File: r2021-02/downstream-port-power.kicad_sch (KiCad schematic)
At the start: 31 parts, among them J10 USB_A_DUAL, J4 USB_A (female down), J6 USB_A_DUAL, J7 USB_A_DUAL, U10 NUP4202, U11 NUP4202, U13 NUP4202, U14 NUP4202, U15 NUP4202, U16 NUP4202, U17 NUP4202, U3 USB2517, U4 APL3511C, U5 APL3511C, U6 APL3511C, U7 APL3511C, U8 APL3511C, U9 APL3511C

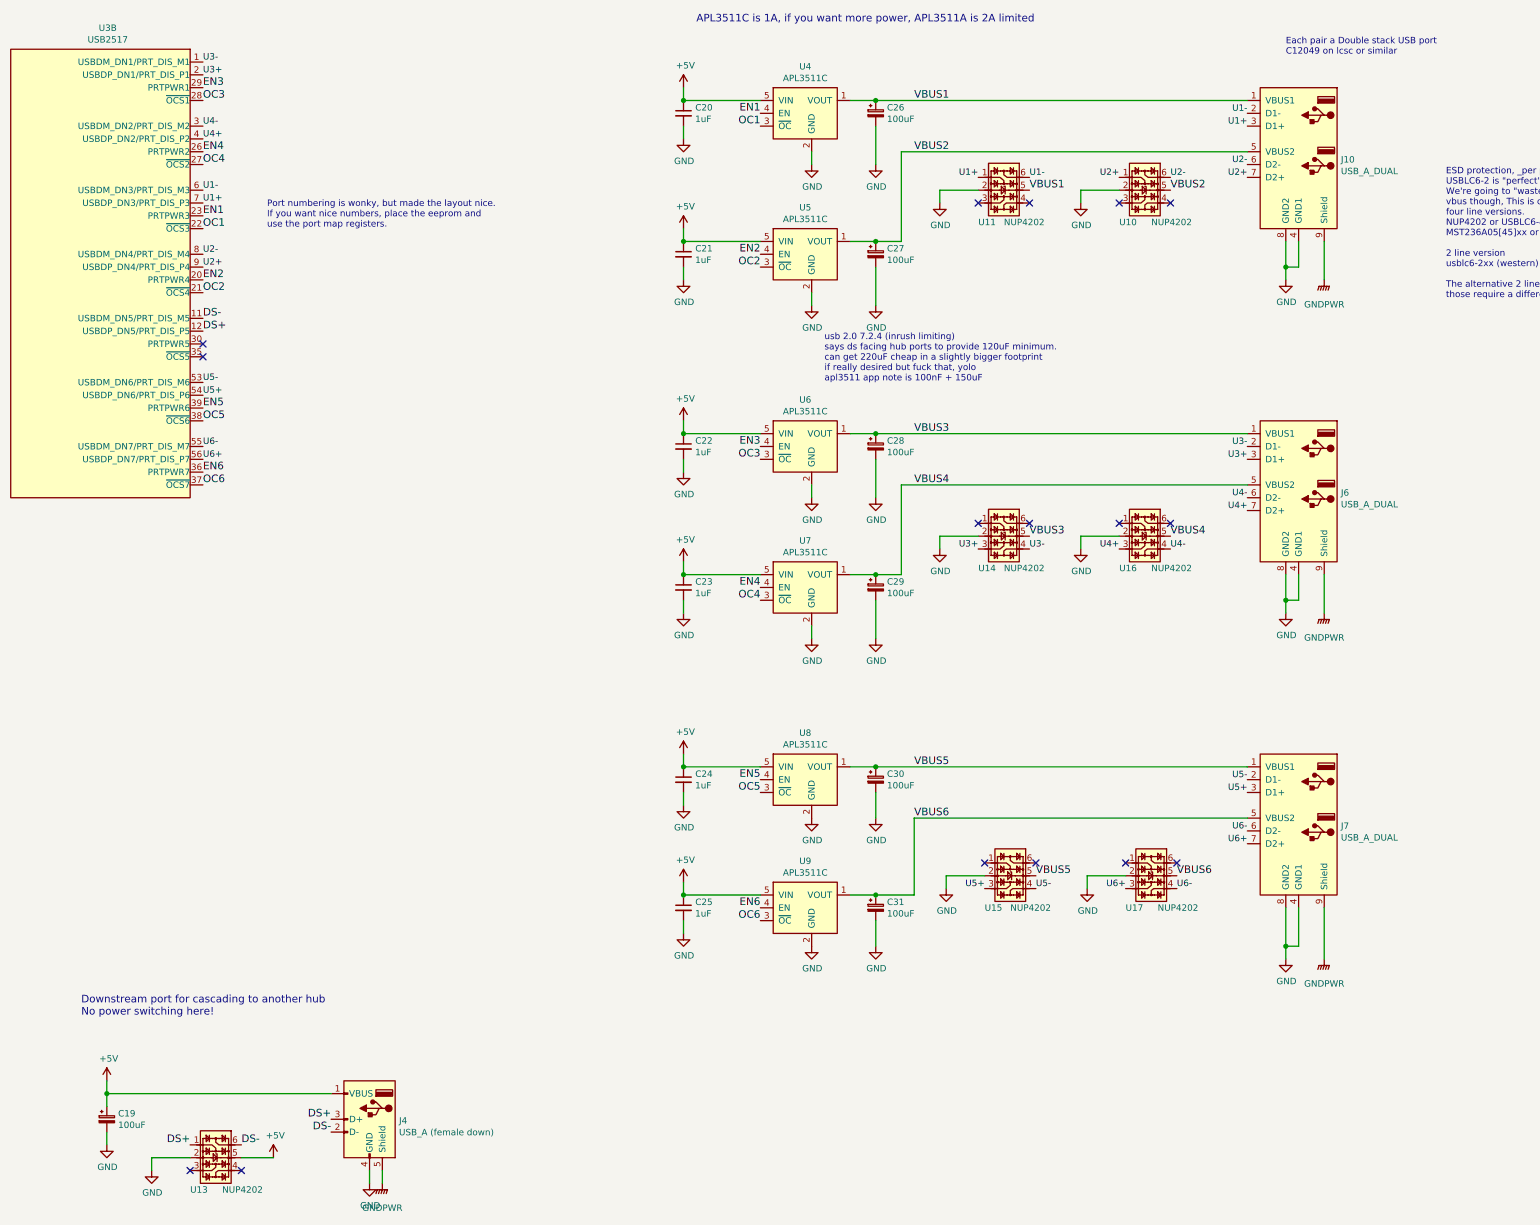
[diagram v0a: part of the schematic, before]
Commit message: switch to upstream dual usb symbol
less private local parts, more better.
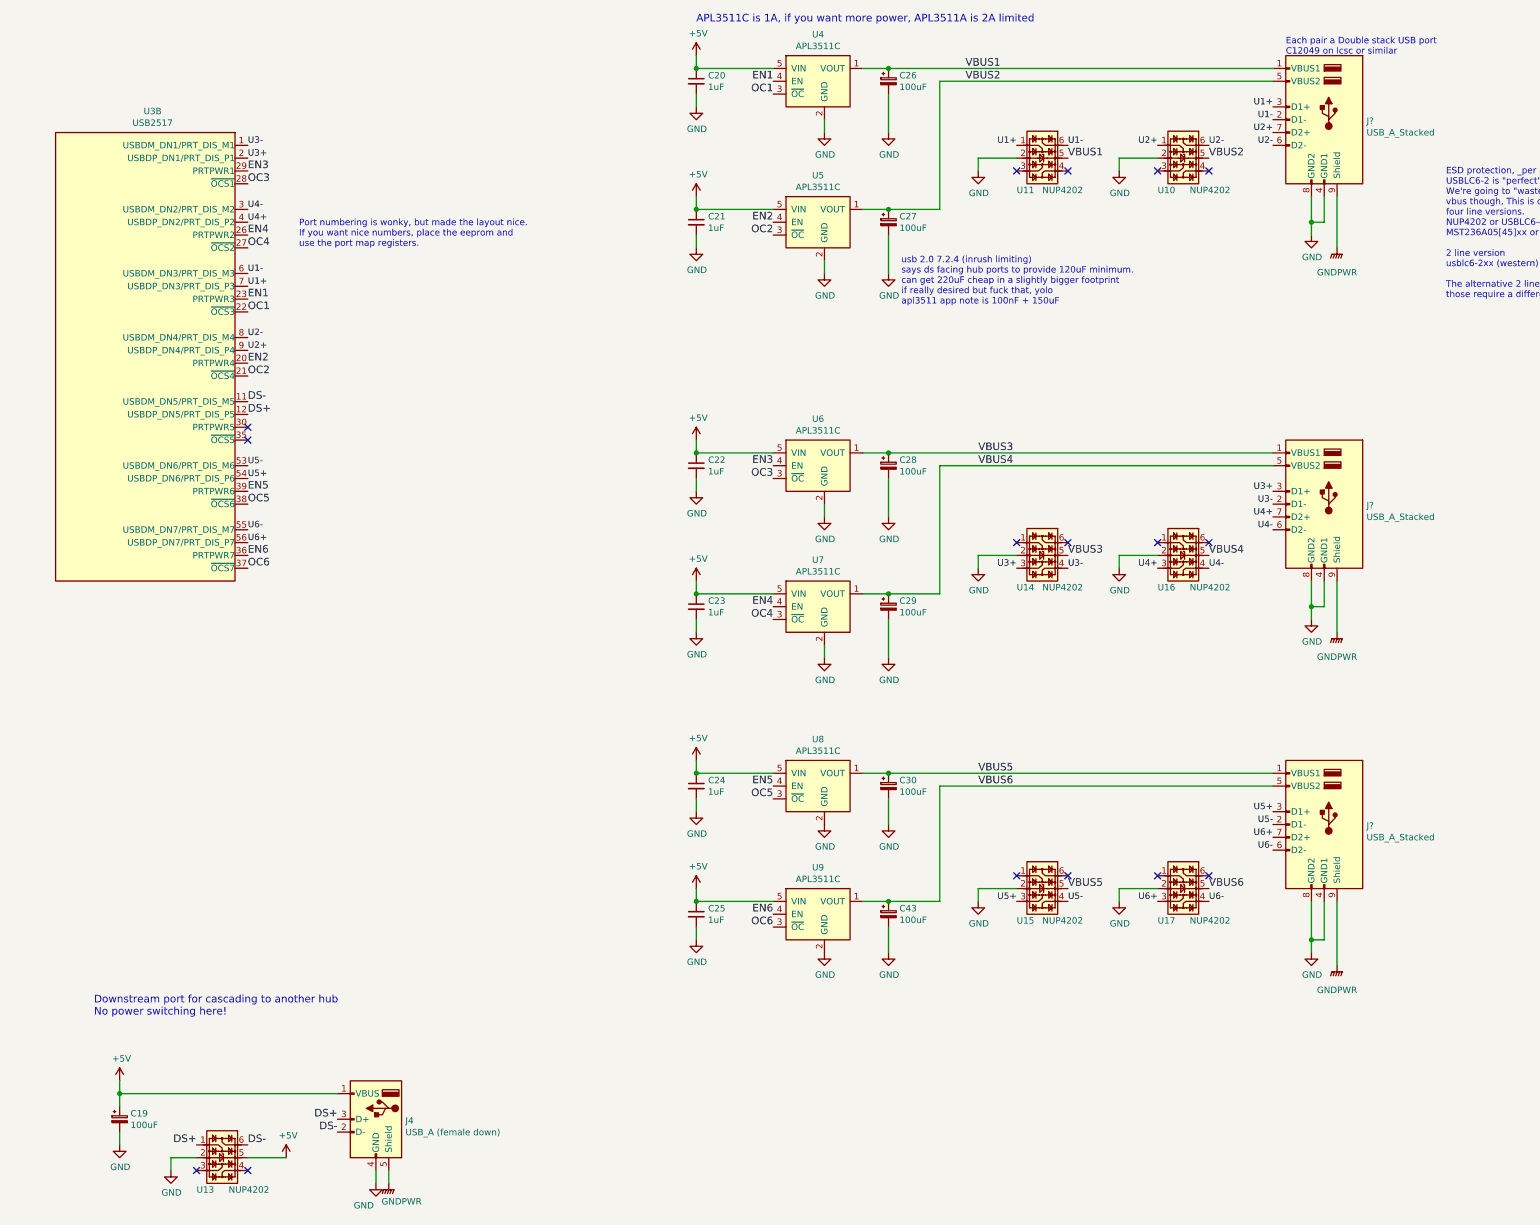
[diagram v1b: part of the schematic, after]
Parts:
- removed C19, C26, C27, C28, C29, C30, C31: 100uF, Capacitor_SMD:CP_Elec_5x5.4, symbol Device:CP_Small
- removed J10, J6, J7: USB_A_DUAL, Connector_USB:USB_A_Wuerth_61400826021_Horizontal_Stacked, symbol Connector:USB_A_DUAL
- added C19, C26, C27, C28, C29, C30, C43: 100uF, Capacitor_SMD:CP_Elec_5x5.4, symbol Device:C_Polarized_Small
- added J? (x3): USB_A_Stacked, symbol Connector:USB_A_Stacked
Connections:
- net +5V: now also C19.1
- net GND: now also C19.2, C26.2, C27.2, C28.2, C29.2, C30.2, C43.2, J?.4 (GND1), J?.4 (GND1), J?.4 (GND1), J?.8 (GND2), J?.8 (GND2), J?.8 (GND2)
- net GNDPWR: now also J?.9 (Shield), J?.9 (Shield), J?.9 (Shield)
- net U1+: now also J?.3 (D1+)
- net U1-: now also J?.2 (D1-)
- net U2+: now also J?.7 (D2+)
- net U2-: now also J?.6 (D2-)
- net U3+: now also J?.3 (D1+)
- net U3-: now also J?.2 (D1-)
- net U4+: now also J?.7 (D2+)
- net U4-: now also J?.6 (D2-)
- net U5+: now also J?.3 (D1+)
- net U5-: now also J?.2 (D1-)
- net U6+: now also J?.7 (D2+)
- net U6-: now also J?.6 (D2-)
- net VBUS1: now also C26.1, J?.1 (VBUS1)
- net VBUS2: now also C27.1, J?.5 (VBUS2)
- net VBUS3: now also C28.1, J?.1 (VBUS1)
- net VBUS4: now also C29.1, J?.5 (VBUS2)
- net VBUS5: now also C30.1, J?.1 (VBUS1)
- net VBUS6: now also C43.1, J?.5 (VBUS2)
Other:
- moved on the sheet: C20, C21, C22, C23, C24, C25, J4, U10, U11, U13, U14, U15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

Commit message: start rev2
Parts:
- added C1: 1uF, Capacitor_SMD:C_0603_1608Metric, symbol Device:C_Small
- added U19: APL3511C, Package_TO_SOT_SMD:SOT-23-5, symbol Power_Management:APL3511C
- J2, J3, J6: renamed from J?; footprint (none) -> Connector_USB:USB_A_Wuerth_61400826021_Horizontal_Stacked
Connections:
- net +5V: now also C1.1, U19.5 (VIN); no longer C19.1, J4.1 (VBUS)
- net GND: now also C1.2, U19.2 (GND)
- net EN_DS: now reaches U3.30 (PRTPWR5)
- net EN_DS: now also U19.4 (EN)
- net OC_DS: now reaches U3.35 (~OCS5)
- net OC_DS: now also U19.3 (~OC)
- new net VBUS_DS: C19.1, J4.1 (VBUS), U19.1 (VOUT)
- no-connect marks 16 -> 14
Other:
- note added: "Downstream port for cascading to another hub Power switching as well, because why not!"
- note removed: "Downstream port for cascading to another hub No power switching here!"
- moved on the sheet: C19, J4, U13

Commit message: hubbish 2021-2 updates
line it up a bit better, realise parts are no longer available, start
kidding myself I'm working on this again.
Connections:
- net +5V: no longer U13.5
- net U2+: now also U10.4; no longer U10.1
- net U2-: now also U10.3; no longer U10.6
- net U3+: now also U14.1; no longer U14.3
- net U3-: now also U14.6; no longer U14.4
- net U4+: now also U16.4; no longer U16.3
- net U4-: now also U16.3; no longer U16.4
- net U5+: now also U15.1; no longer U15.3
- net U5-: now also U15.6; no longer U15.4
- net U6+: now also U17.4; no longer U17.3
- net U6-: now also U17.3; no longer U17.4
- net VBUS_DS: now also U13.5

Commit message: restore to kicad 6.0 compatibility
updated to my footprintbranch, 6.0 and all that
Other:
- note added: "APL3511C is 1A, if you want more power, APL3511A is 2A limited Pin Compatible: Diodes AP22811AW5 (2A) (W5 is case, sot23, A is active high) Diodes AP2171DWG and AP2171WG (1A) (W is case) STMPS2171STR (1A)"
- note removed: "APL3511C is 1A, if you want more power, APL3511A is 2A limited"

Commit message: overhaul, push silk, complete "again"
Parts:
- renumbered C1 to C26, C19 to C27, C26 to C28, C27 to C29, C28 to C30, C29 to C31, C30 to C32, C43 to C33, J2 to J5, J3 to J6, J6 to J7, U19 to U10, U13 to U11, U11 to U12, U14 to U13, U15 to U14, U10 to U15
